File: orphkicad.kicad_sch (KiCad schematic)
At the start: 41 parts, among them J1 USB_C_Receptacle_USB2.0_16P, SW1 BTN_BOOT, SW2 BTN_RST, SW3 BTN_USR, U1 RP2040, U2 W25Q16JVUXIQ, U3 USBLC6-2SC6, U5 XC6206PxxxMR, X1 X322512MSB4SI

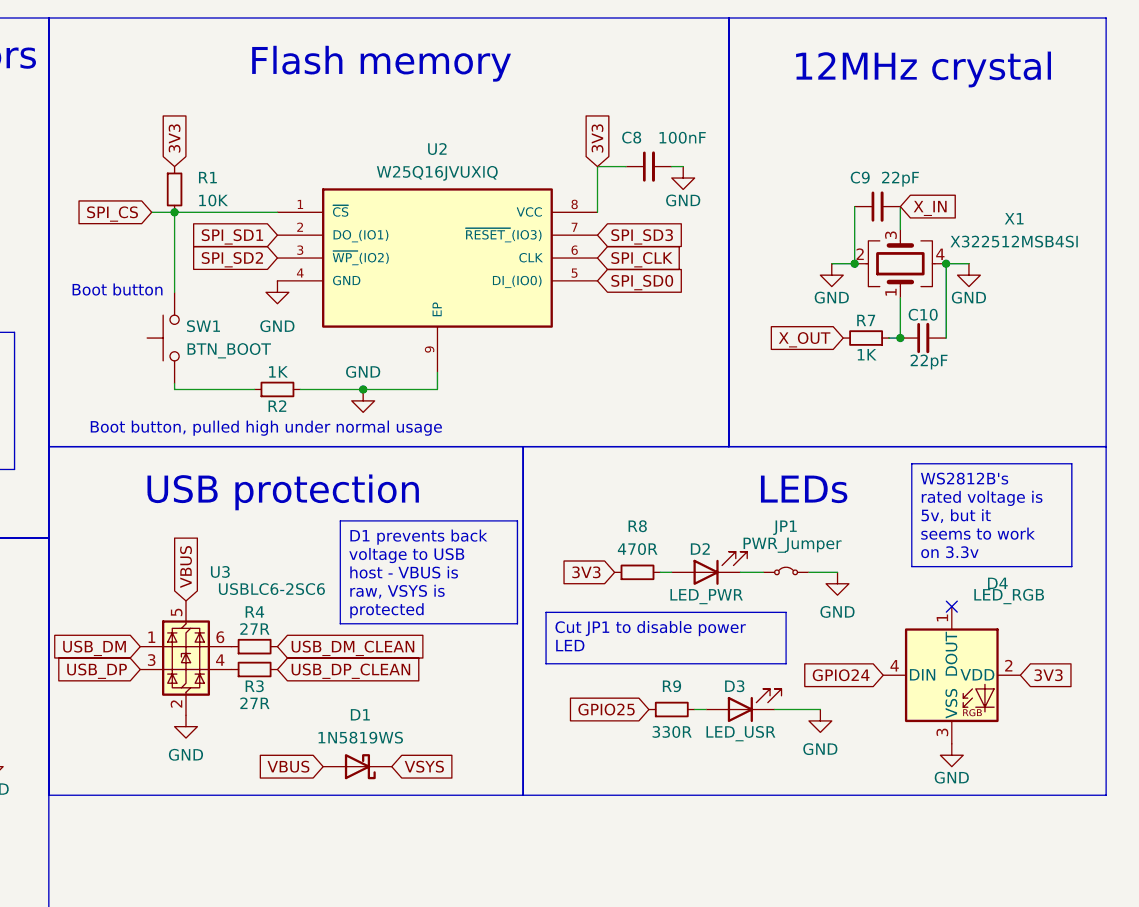
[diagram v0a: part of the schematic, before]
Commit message: Merge resistors, dim LED, change crystal
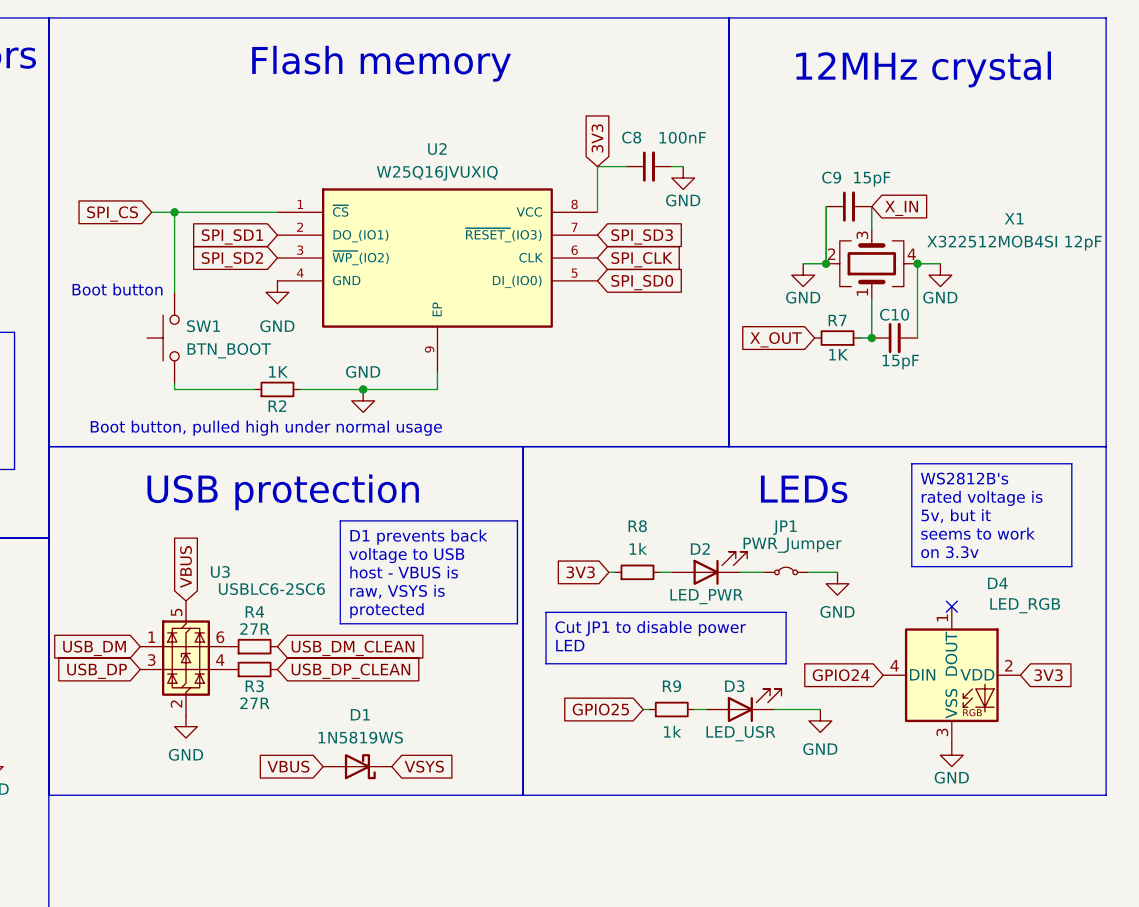
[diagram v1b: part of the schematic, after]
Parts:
- removed R1: 10K, Resistor_SMD:R_0402_1005Metric, symbol Device:R_Small
- C10, C9: value 22pF -> 15pF
- R8: value 470R -> 1k
- R9: value 330R -> 1k
- X1: value X322512MSB4SI -> X322512MOB4SI 12pF
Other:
- moved on the sheet: C10, C9, R7, X1
